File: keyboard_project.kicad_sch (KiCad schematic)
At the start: 198 parts, among them J1 USB_C_Receptacle_USB2.0, J2 Conn_01x04, J3 Conn_01x05, SW1 SW_Push, SW2 SW_Push, U1 RP2040, U2 XC6206PxxxMR, U3 SRV05-4, U4 W25Q128JVS, Y1 Crystal_GND24

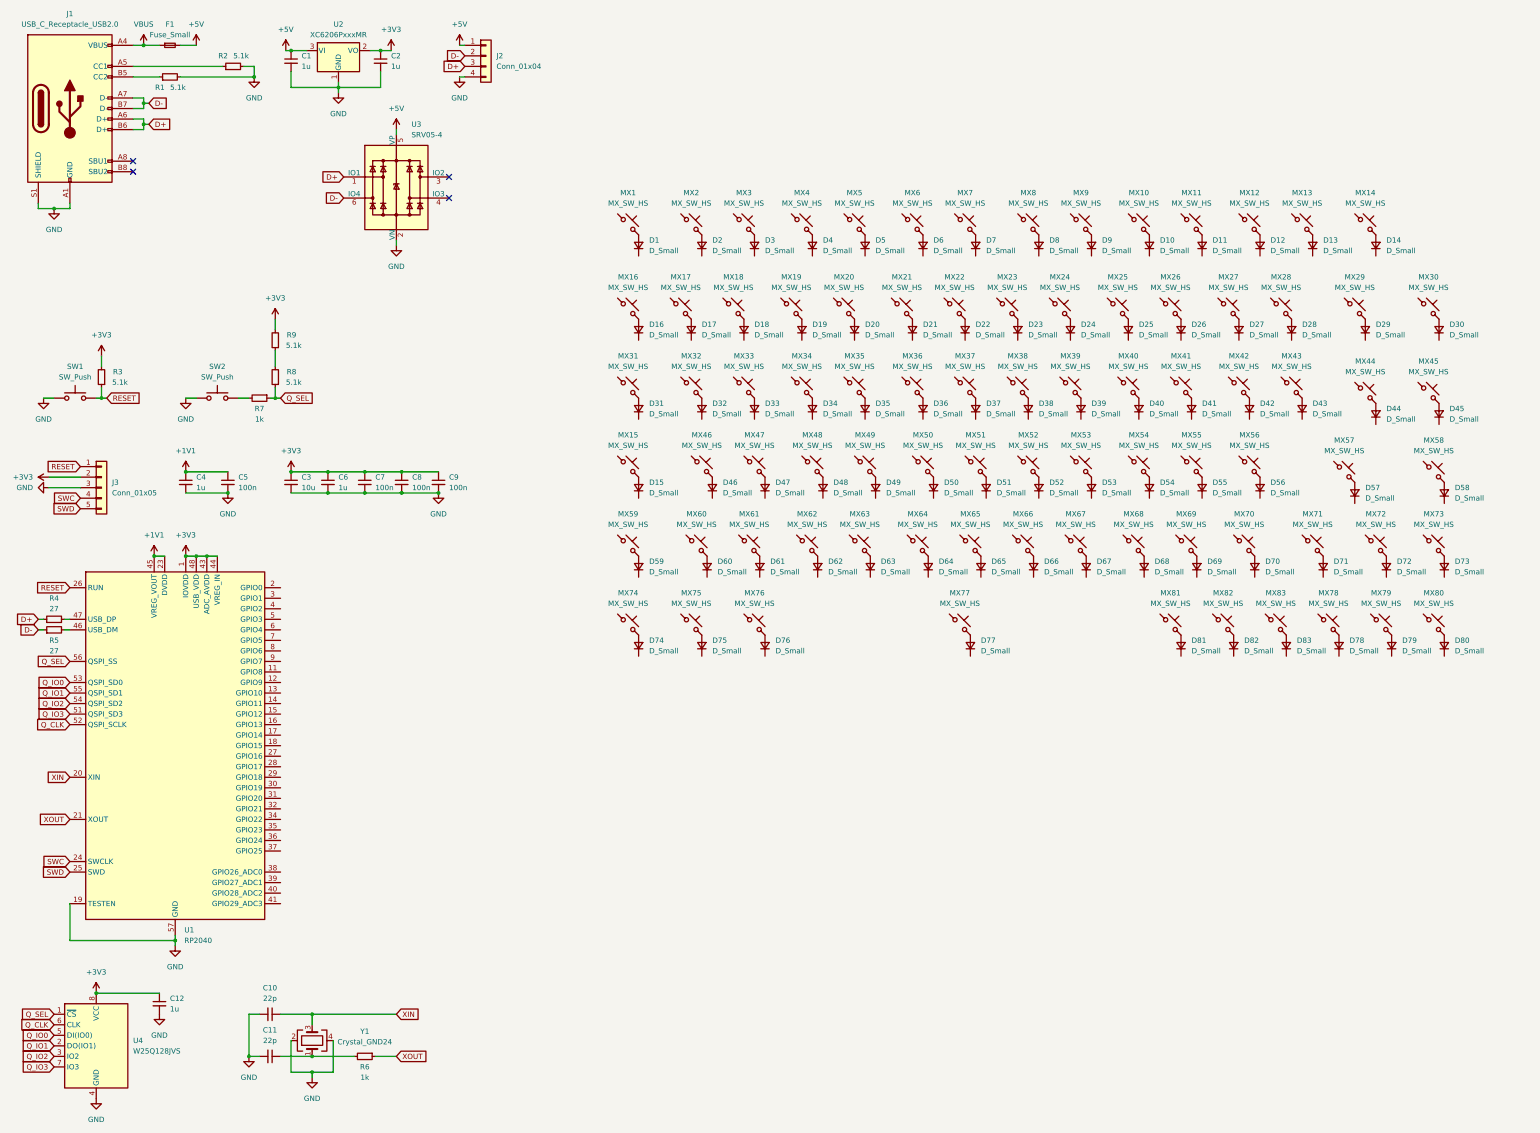
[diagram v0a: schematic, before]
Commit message: Added footprints to components
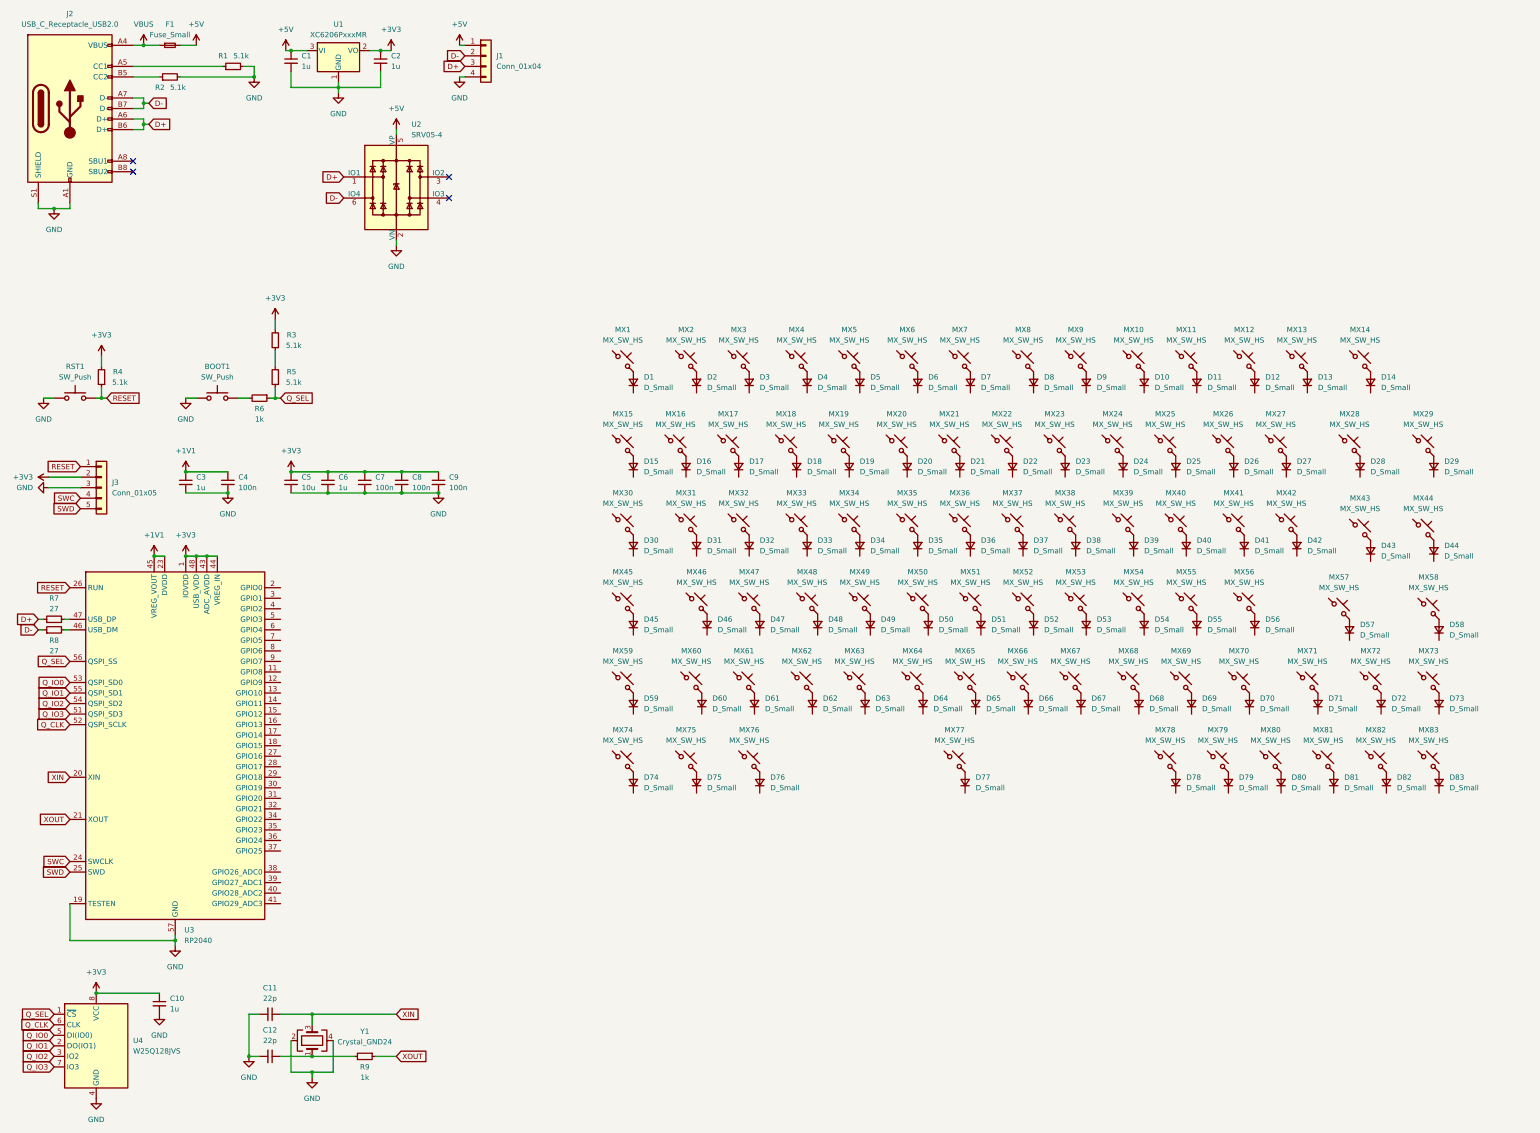
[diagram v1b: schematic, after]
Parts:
- BOOT1: renamed from SW2; footprint (none) -> Button_Switch_SMD:SW_SPST_TL3342
- C1, C2, C6, C7, C8, C9: footprint (none) -> Capacitor_SMD:C_0402_1005Metric
- C10: renamed from C12; footprint (none) -> Capacitor_SMD:C_0402_1005Metric
- C11: renamed from C10; footprint (none) -> Capacitor_SMD:C_0402_1005Metric
- C12: renamed from C11; footprint (none) -> Capacitor_SMD:C_0402_1005Metric
- C3: renamed from C4; footprint (none) -> Capacitor_SMD:C_0402_1005Metric
- C4: renamed from C5; footprint (none) -> Capacitor_SMD:C_0402_1005Metric
- C5: renamed from C3; footprint (none) -> Capacitor_SMD:C_0603_1608Metric
- D1, D10, D11, D12, D13, D14, D2, D3, D4, D46, D47, D48, D49, D5, D50, D51, D52, D53, D54, D55, D56, D57, D58, D59, D6, D60, D61, D62, D63, D64, D65, D66, D67, D68, D69, D7, D70, D71, D72, D73, D74, D75, D76, D77, D8, D9: footprint (none) -> Diode_SMD:D_SOD-123
- D15: renamed from D16; footprint (none) -> Diode_SMD:D_SOD-123
- D16: renamed from D17; footprint (none) -> Diode_SMD:D_SOD-123
- D17: renamed from D18; footprint (none) -> Diode_SMD:D_SOD-123
- D18: renamed from D19; footprint (none) -> Diode_SMD:D_SOD-123
- D19: renamed from D20; footprint (none) -> Diode_SMD:D_SOD-123
- D20: renamed from D21; footprint (none) -> Diode_SMD:D_SOD-123
- D21: renamed from D22; footprint (none) -> Diode_SMD:D_SOD-123
- D22: renamed from D23; footprint (none) -> Diode_SMD:D_SOD-123
- D23: renamed from D24; footprint (none) -> Diode_SMD:D_SOD-123
- D24: renamed from D25; footprint (none) -> Diode_SMD:D_SOD-123
- D25: renamed from D26; footprint (none) -> Diode_SMD:D_SOD-123
- D26: renamed from D27; footprint (none) -> Diode_SMD:D_SOD-123
- D27: renamed from D28; footprint (none) -> Diode_SMD:D_SOD-123
- D28: renamed from D29; footprint (none) -> Diode_SMD:D_SOD-123
- D29: renamed from D30; footprint (none) -> Diode_SMD:D_SOD-123
- D30: renamed from D31; footprint (none) -> Diode_SMD:D_SOD-123
- D31: renamed from D32; footprint (none) -> Diode_SMD:D_SOD-123
- D32: renamed from D33; footprint (none) -> Diode_SMD:D_SOD-123
- D33: renamed from D34; footprint (none) -> Diode_SMD:D_SOD-123
- D34: renamed from D35; footprint (none) -> Diode_SMD:D_SOD-123
- D35: renamed from D36; footprint (none) -> Diode_SMD:D_SOD-123
- D36: renamed from D37; footprint (none) -> Diode_SMD:D_SOD-123
- D37: renamed from D38; footprint (none) -> Diode_SMD:D_SOD-123
- D38: renamed from D39; footprint (none) -> Diode_SMD:D_SOD-123
- D39: renamed from D40; footprint (none) -> Diode_SMD:D_SOD-123
- D40: renamed from D41; footprint (none) -> Diode_SMD:D_SOD-123
- D41: renamed from D42; footprint (none) -> Diode_SMD:D_SOD-123
- D42: renamed from D43; footprint (none) -> Diode_SMD:D_SOD-123
- D43: renamed from D44; footprint (none) -> Diode_SMD:D_SOD-123
- D44: renamed from D45; footprint (none) -> Diode_SMD:D_SOD-123
- D45: renamed from D15; footprint (none) -> Diode_SMD:D_SOD-123
- D78: renamed from D81; footprint (none) -> Diode_SMD:D_SOD-123
- D79: renamed from D82; footprint (none) -> Diode_SMD:D_SOD-123
- D80: renamed from D83; footprint (none) -> Diode_SMD:D_SOD-123
- D81: renamed from D78; footprint (none) -> Diode_SMD:D_SOD-123
- D82: renamed from D79; footprint (none) -> Diode_SMD:D_SOD-123
- D83: renamed from D80; footprint (none) -> Diode_SMD:D_SOD-123
- F1: footprint (none) -> Fuse:Fuse_1206_3216Metric
- J1: renamed from J2; footprint (none) -> Connector_JST:JST_SH_SM04B-SRSS-TB_1x04-1MP_P1.00mm_Horizontal
- J2: renamed from J1; footprint (none) -> Connector_USB:USB_C_Receptacle_HRO_TYPE-C-31-M-12
- J3: footprint (none) -> Connector_PinHeader_2.54mm:PinHeader_1x05_P2.54mm_Vertical
- R1: renamed from R2; footprint (none) -> Resistor_SMD:R_0402_1005Metric
- R2: renamed from R1; footprint (none) -> Resistor_SMD:R_0402_1005Metric
- R3: renamed from R9; footprint (none) -> Resistor_SMD:R_0402_1005Metric
- R4: renamed from R3; footprint (none) -> Resistor_SMD:R_0402_1005Metric
- R5: renamed from R8; footprint (none) -> Resistor_SMD:R_0402_1005Metric
- R6: renamed from R7; footprint (none) -> Resistor_SMD:R_0402_1005Metric
- R7: renamed from R4; footprint (none) -> Resistor_SMD:R_0402_1005Metric
- R8: renamed from R5; footprint (none) -> Resistor_SMD:R_0402_1005Metric
- R9: renamed from R6; footprint (none) -> Resistor_SMD:R_0402_1005Metric
- RST1: renamed from SW1; footprint (none) -> Button_Switch_SMD:SW_SPST_TL3342
- Y1: footprint (none) -> Crystal:Crystal_SMD_3225-4Pin_3.2x2.5mm
- renumbered MX16 to MX15, MX17 to MX16, MX18 to MX17, MX19 to MX18, MX20 to MX19, MX21 to MX20, MX22 to MX21, MX23 to MX22, MX24 to MX23, MX25 to MX24, MX26 to MX25, MX27 to MX26, MX28 to MX27, MX29 to MX28, MX30 to MX29, MX31 to MX30, MX32 to MX31, MX33 to MX32, MX34 to MX33, MX35 to MX34, MX36 to MX35, MX37 to MX36, MX38 to MX37, MX39 to MX38, MX40 to MX39, MX41 to MX40, MX42 to MX41, MX43 to MX42, MX44 to MX43, MX45 to MX44, MX15 to MX45, MX81 to MX78, MX82 to MX79, MX83 to MX80, MX78 to MX81, MX79 to MX82, MX80 to MX83, U2 to U1, U3 to U2, U1 to U3
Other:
- moved on the sheet: D1, D10, D11, D12, D13, D14, D15, D16, D17, D18, D19, D2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

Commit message: Basics schematics done, PCB design started
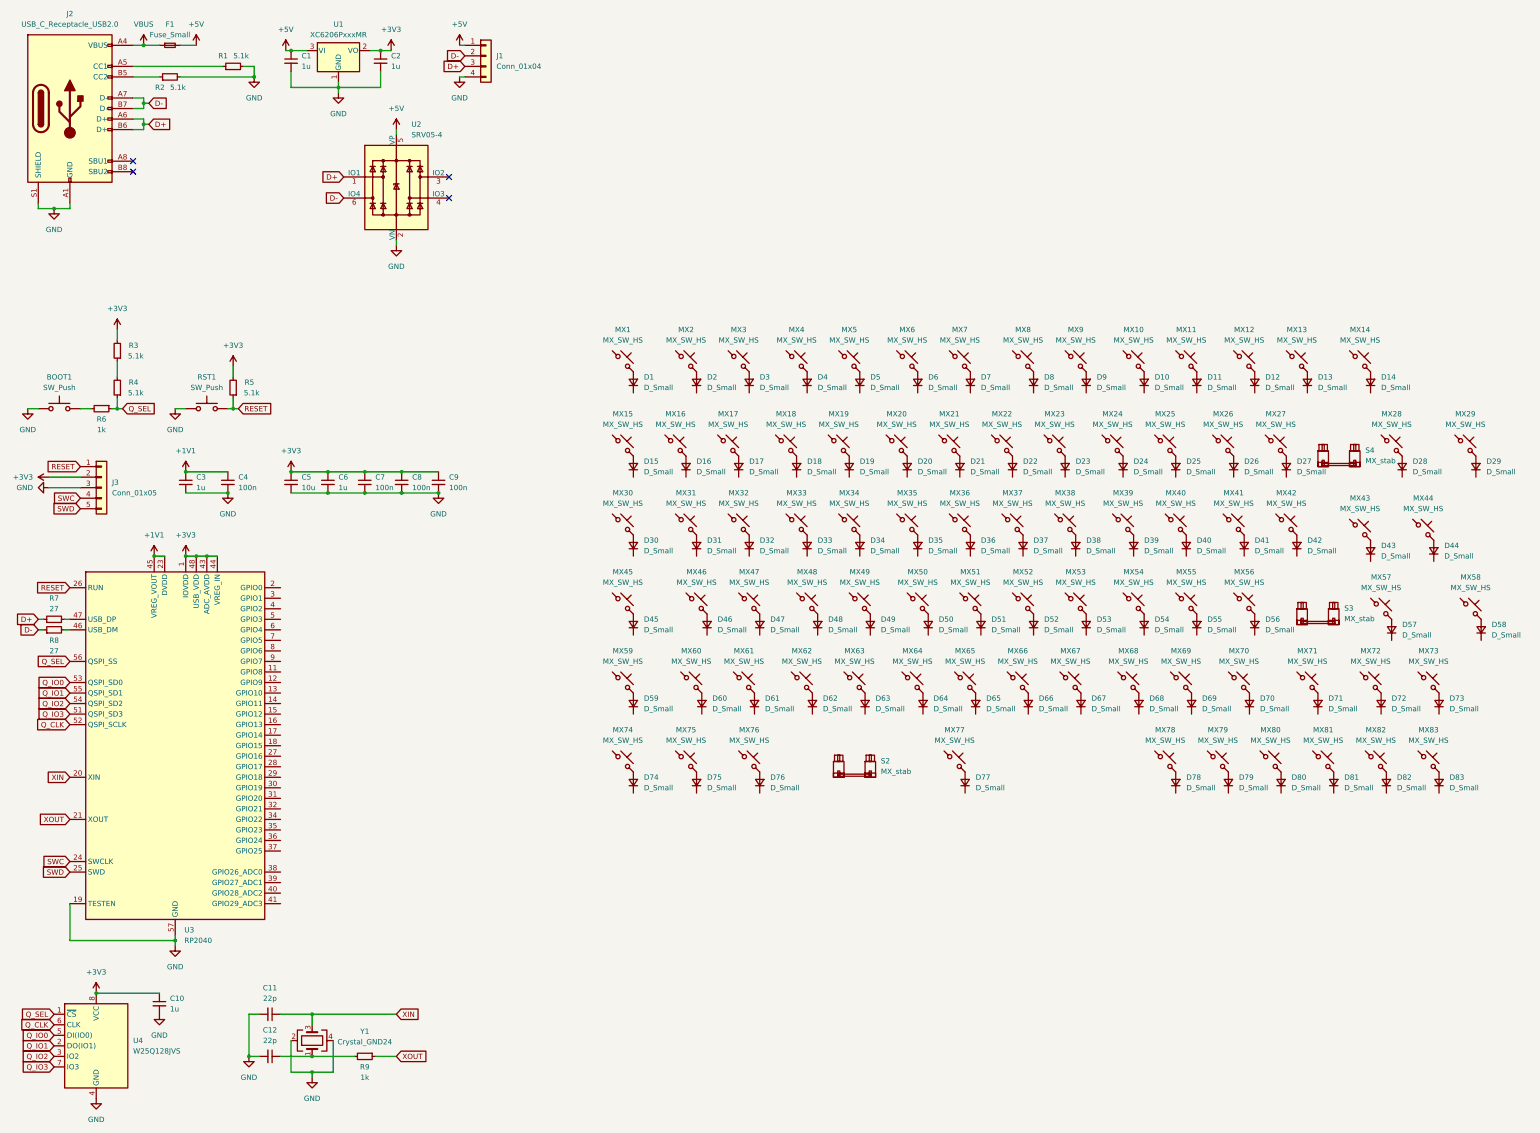
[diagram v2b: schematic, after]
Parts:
- added S2: MX_stab, PCM_marbastlib-mx:STAB_MX_P_6.25u, symbol PCM_marbastlib-mx:MX_stab
- added S3: MX_stab, PCM_marbastlib-mx:STAB_MX_P_2.25u, symbol PCM_marbastlib-mx:MX_stab
- added S4: MX_stab, PCM_marbastlib-mx:STAB_MX_P_2u, symbol PCM_marbastlib-mx:MX_stab
- MX30, MX43: footprint PCM_marbastlib-mx:SW_MX_HS_1u -> PCM_marbastlib-mx:SW_MX_HS_1.5u
- MX45, MX71: footprint PCM_marbastlib-mx:SW_MX_HS_1u -> PCM_marbastlib-mx:SW_MX_HS_1.75u
- MX59, MX74, MX75, MX76: footprint PCM_marbastlib-mx:SW_MX_HS_1u -> PCM_marbastlib-mx:SW_MX_HS_1.25u
- renumbered R5 to R4, R4 to R5
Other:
- moved on the sheet: BOOT1, D28, D29, D57, D58, MX28, MX29, MX57, MX58, R3, R4, R5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
